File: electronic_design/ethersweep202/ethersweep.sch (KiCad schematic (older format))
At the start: 88 parts, among them J1 AVR-ISP-6, J10 HR911105A, J2 Conn_01x02_Male, J3 Conn_01x04_Female, J4 Conn_01x02_Male, J5 Conn_01x02_Male, J7 Conn_01x06_Female, J8 AVR-ISP-6, J9 Conn_01x06_Male, M1 Stepper_Motor_bipolar, SW1 SW_Push, U2 ATmega328-AU, U3 DRV8825PWPR, U4 AMS1117-3.3, U5 AS5600, U6 W5500, Y2 Crystal_25MHz, Y3 Crystal

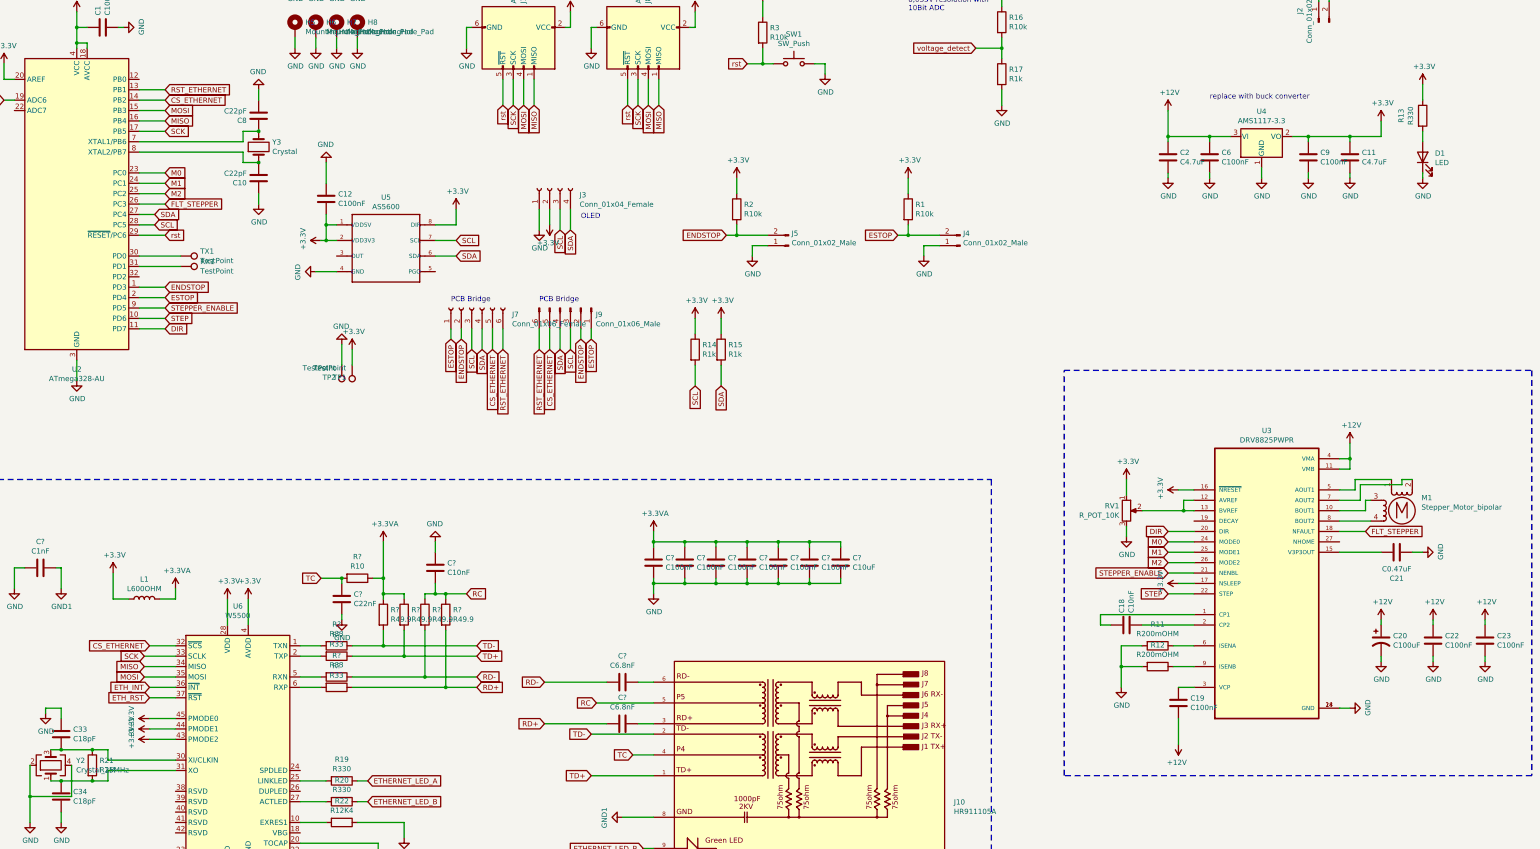
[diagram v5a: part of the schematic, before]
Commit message: added interrupt pin to w5500
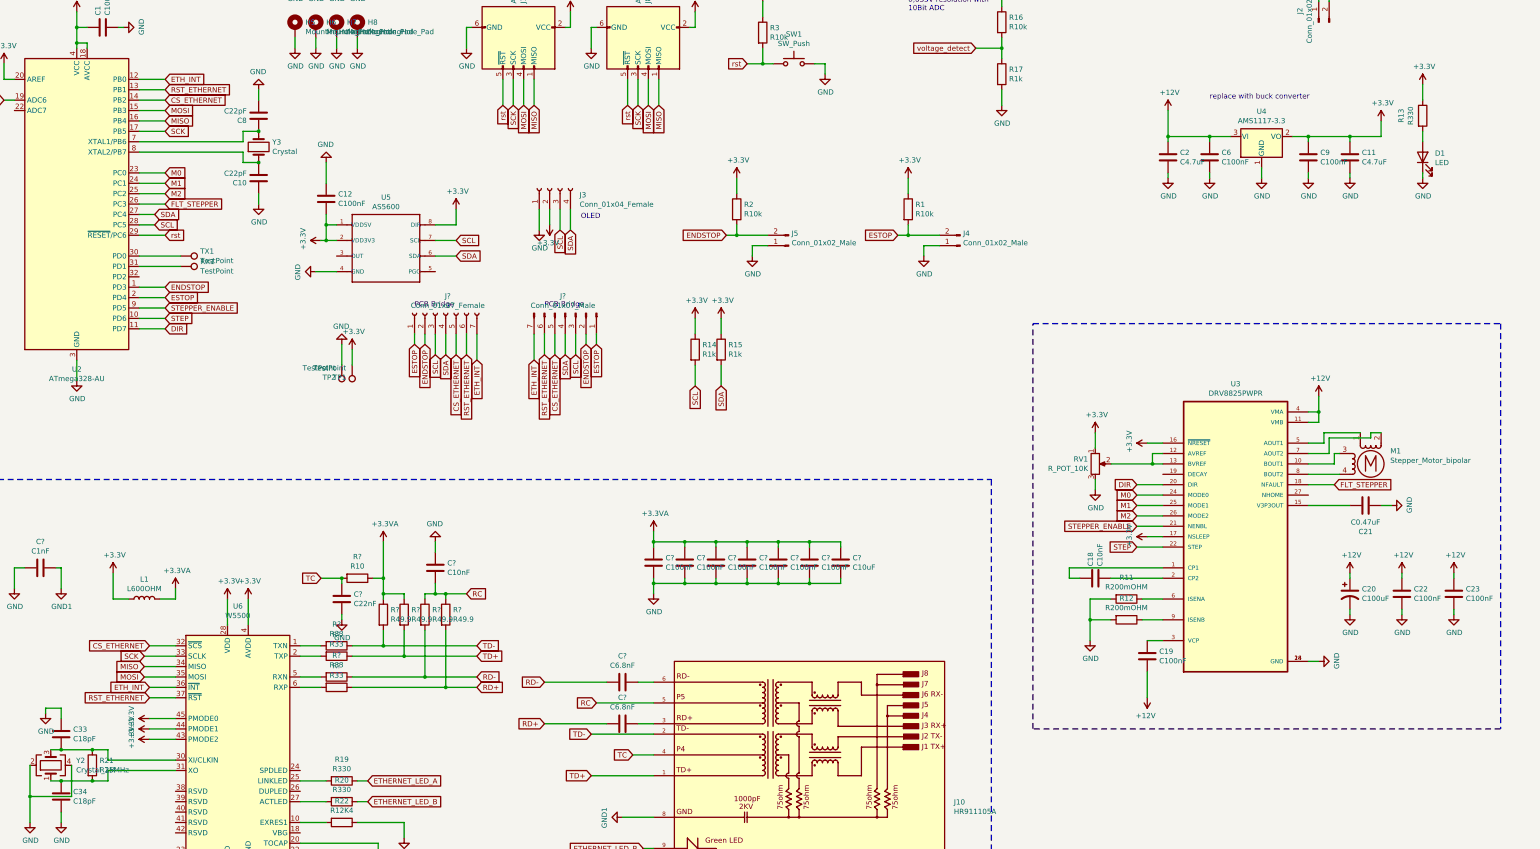
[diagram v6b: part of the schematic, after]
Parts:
- removed J7: Conn_01x06_Female, Connector_PinHeader_2.54mm:PinHeader_1x06_P2.54mm_Vertical, symbol Connector:Conn_01x06_Female
- removed J9: Conn_01x06_Male, Connector_PinHeader_2.54mm:PinHeader_1x06_P2.54mm_Vertical, symbol Connector:Conn_01x06_Male
- added J?: Conn_01x07_Male, symbol Connector:Conn_01x07_Male
- added J?: Conn_01x07_Female, symbol Connector:Conn_01x07_Female
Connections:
- net ETH_RST is gone; now on net RST_ETHERNET: U6.37 (~RST)
- net CS_ETHERNET: now also J?.5 (Pin_5), J?.5 (Pin_5)
- net ENDSTOP: now also J?.2 (Pin_2), J?.2 (Pin_2)
- net ESTOP: now also J?.1 (Pin_1), J?.1 (Pin_1)
- net ETH_INT: now also U2.12 (PB0), J?.7 (Pin_7), J?.7 (Pin_7)
- net RST_ETHERNET: now also J?.6 (Pin_6), J?.6 (Pin_6)
- net SCL: now also J?.3 (Pin_3), J?.3 (Pin_3)
- net SDA: now also J?.4 (Pin_4), J?.4 (Pin_4)
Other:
- moved on the sheet: C18, C19, C20, C21, C22, C23, M1, R11, R12, RV1, U3

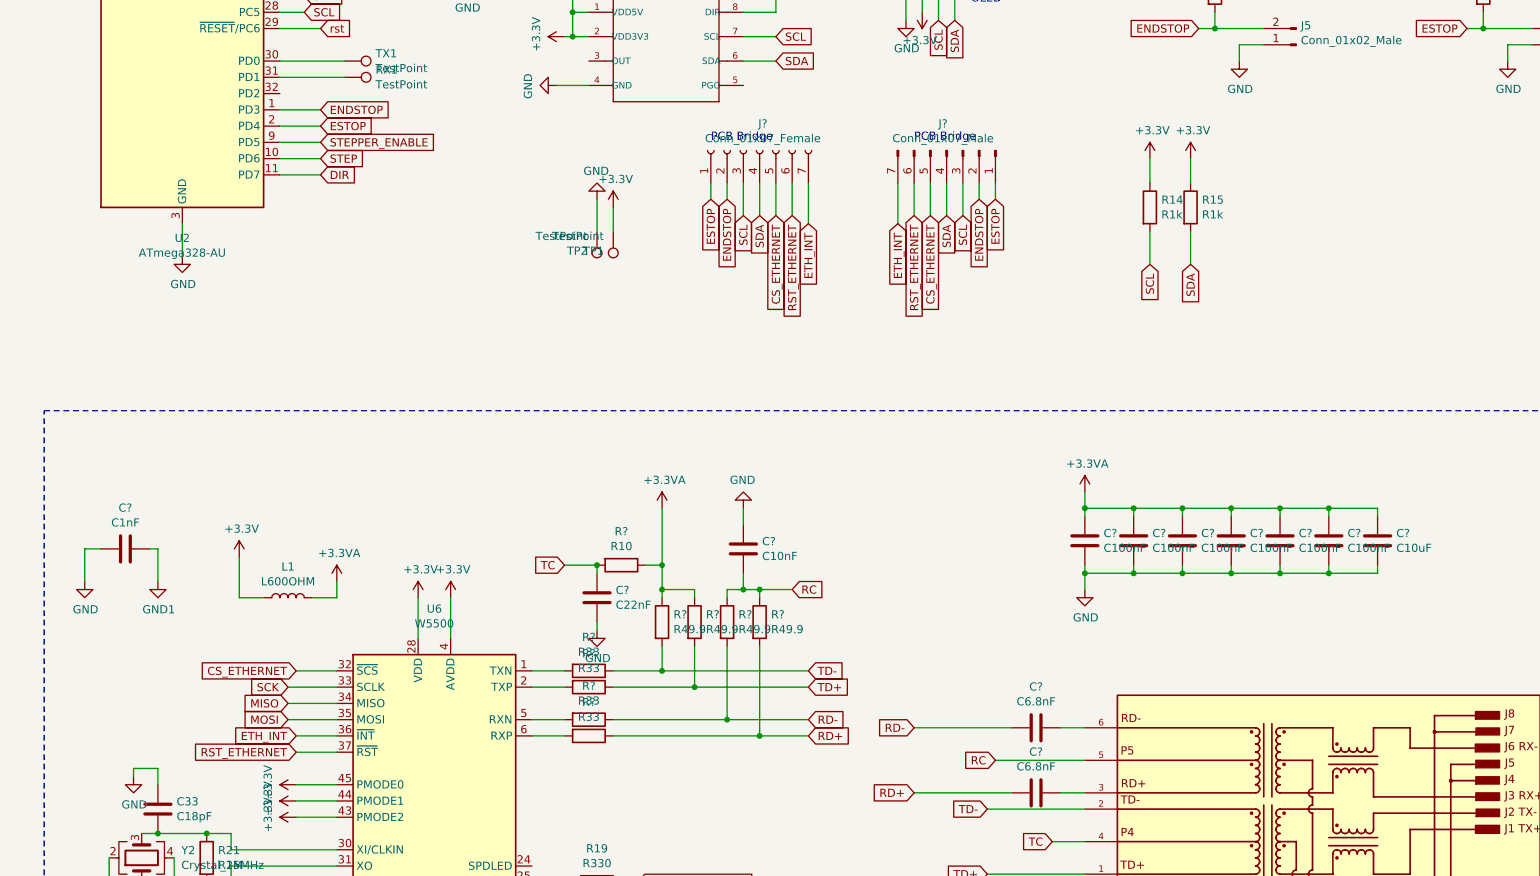
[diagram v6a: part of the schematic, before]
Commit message: layout implementation board 1 done, board 2 in progress
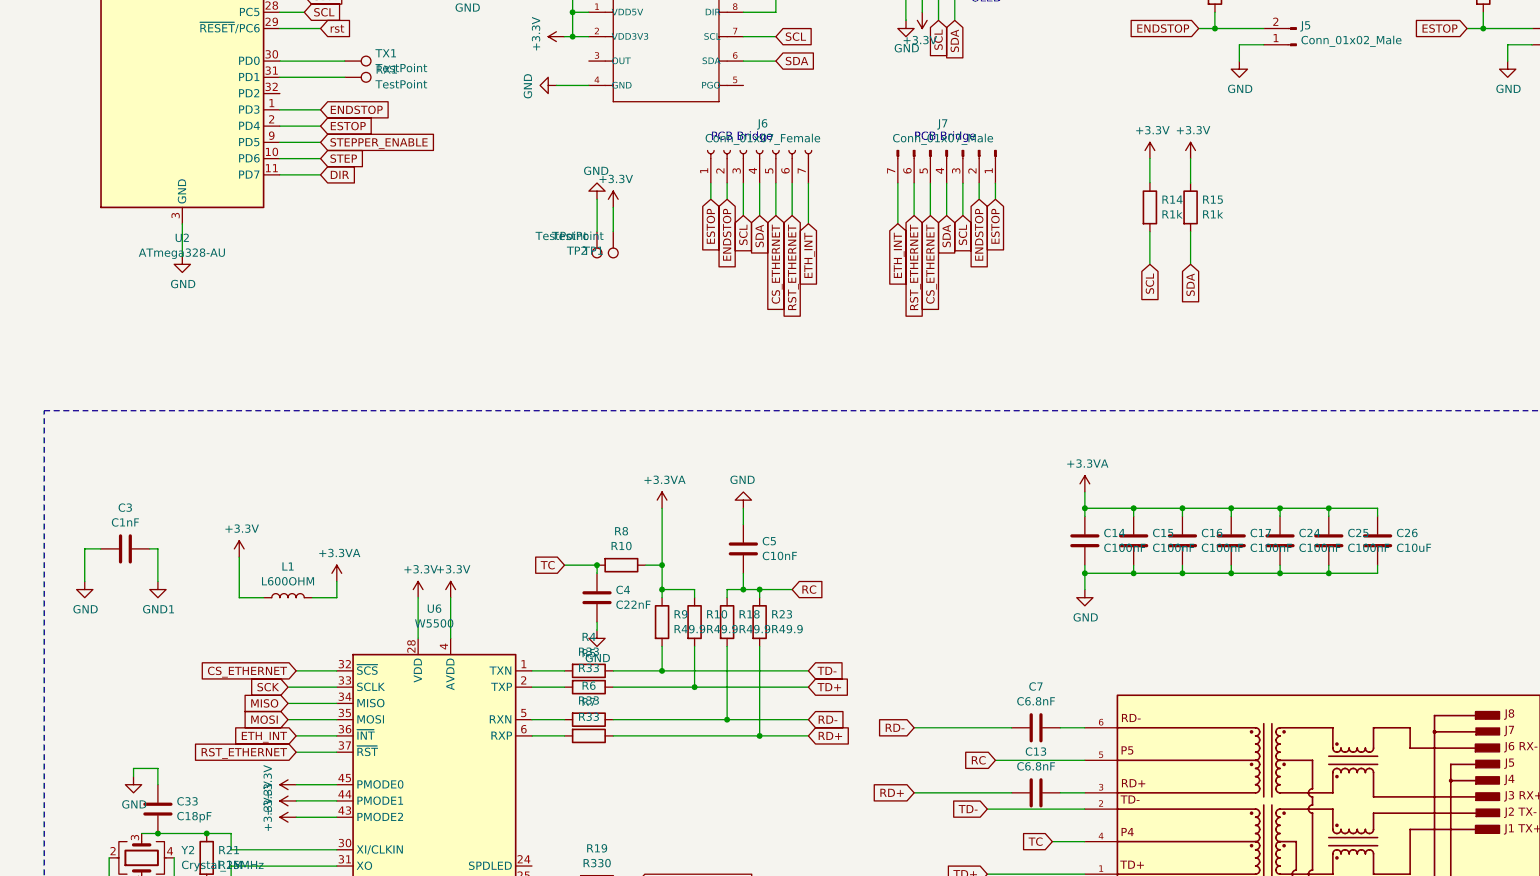
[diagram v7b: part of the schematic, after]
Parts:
- J6, J7: renamed from J?; footprint (none) -> Connector_PinHeader_2.54mm:PinHeader_1x07_P2.54mm_Vertical
- L1: footprint (none) -> Inductor_SMD:L_0805_2012Metric
- gave numbers to parts that had none: 21
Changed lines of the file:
@@
 F 0 "L1" V 2790 6950 50  0000 C CNN
 F 1 "L600OHM" V 2699 6950 50  0000 C CNN
-F 2 "" H 2600 6950 50  0001 C CNN
+F 2 "Inductor_SMD:L_0805_2012Metric" H 2600 6950 50  0001 C CNN
 F 3 "~" H 2600 6950 50  0001 C CNN
 F 4 "C1017" V 2600 6950 50  0001 C CNN "LCSC"
@@
 	5100 9100 5100 9250
 $Comp
-L power:GND1 #PWR?
+L power:GND1 #PWR0109
 U 1 1 614FEAD4
 P 1800 6850
-F 0 "#PWR?" H 1800 6600 50  0001 C CNN
+F 0 "#PWR0109" H 1800 6600 50  0001 C CNN
 F 1 "GND1" H 1805 6677 50  0000 C CNN
 F 2 "" H 1800 6850 50  0001 C CNN
@@
 $EndComp
 $Comp
-L power:GND #PWR?
+L power:GND #PWR0115
 U 1 1 6152709E
 P 1350 6850
-F 0 "#PWR?" H 1350 6600 50  0001 C CNN
+F 0 "#PWR0115" H 1350 6600 50  0001 C CNN
 F 1 "GND" H 1355 6677 50  0000 C CNN
 F 2 "" H 1350 6850 50  0001 C CNN
@@
 $EndComp
 $Comp
-L Device:C C?
+L Device:C C3
 U 1 1 61578613
 P 1600 6650
-F 0 "C?" V 1348 6650 50  0000 C CNN
+F 0 "C3" V 1348 6650 50  0000 C CNN
 F 1 "C1nF" V 1439 6650 50  0000 C CNN
 F 2 "Resistor_SMD:R_1206_3216Metric" H 1638 6500 50  0001 C CNN
@@
 	1800 6650 1800 6850
 $Comp
-L Device:C C?
+L Device:C C13
 U 1 1 615FC292
 P 7200 8150
-F 0 "C?" V 6948 8150 50  0000 C CNN
+F 0 "C13" V 6948 8150 50  0000 C CNN
 F 1 "C6.8nF" V 7039 8150 50  0000 C CNN
 F 2 "Resistor_SMD:R_0402_1005Metric" H 7238 8000 50  0001 C CNN
@@
 $EndComp
 $Comp
-L Device:C C?
+L Device:C C7
 U 1 1 615FE6F7
 P 7200 7750
-F 0 "C?" V 6948 7750 50  0000 C CNN
+F 0 "C7" V 6948 7750 50  0000 C CNN
 F 1 "C6.8nF" V 7039 7750 50  0000 C CNN
 F 2 "Resistor_SMD:R_0402_1005Metric" H 7238 7600 50  0001 C CNN
@@
 	7350 8150 7500 8150
 $Comp
-L Device:R R?
+L Device:R R4
 U 1 1 6179C9A4
 P 4450 7400
-F 0 "R?" V 4243 7400 50  0000 C CNN
+F 0 "R4" V 4243 7400 50  0000 C CNN
 F 1 "R33" V 4334 7400 50  0000 C CNN
 F 2 "Resistor_SMD:R_0805_2012Metric" V 4380 7400 50  0001 C CNN
@@
 $EndComp
 $Comp
-L Device:R R?
+L Device:R R5
 U 1 1 6179EB6B
 P 4450 7500
-F 0 "R?" V 4243 7500 50  0000 C CNN
+F 0 "R5" V 4243 7500 50  0000 C CNN
 F 1 "R33" V 4334 7500 50  0000 C CNN
 F 2 "Resistor_SMD:R_0805_2012Metric" V 4380 7500 50  0001 C CNN
@@
 $EndComp
 $Comp
-L Device:R R?
+L Device:R R6
 U 1 1 617C8079
 P 4450 7700
-F 0 "R?" V 4243 7700 50  0000 C CNN
+F 0 "R6" V 4243 7700 50  0000 C CNN
 F 1 "R33" V 4334 7700 50  0000 C CNN
 F 2 "Resistor_SMD:R_0805_2012Metric" V 4380 7700 50  0001 C CNN
@@
 $EndComp
 $Comp
-L Device:R R?
+L Device:R R7
 U 1 1 617C8080
 P 4450 7800
-F 0 "R?" V 4243 7800 50  0000 C CNN
+F 0 "R7" V 4243 7800 50  0000 C CNN
 F 1 "R33" V 4334 7800 50  0000 C CNN
 F 2 "Resistor_SMD:R_0805_2012Metric" V 4380 7800 50  0001 C CNN
@@
 	4300 7800 4100 7800
 $Comp
-L Device:R R?
+L Device:R R10
 U 1 1 618C73B2
 P 5100 7100
-F 0 "R?" H 5170 7146 50  0000 L CNN
+F 0 "R10" H 5170 7146 50  0000 L CNN
 F 1 "R49.9" H 5170 7055 50  0000 L CNN
 F 2 "Resistor_SMD:R_0603_1608Metric" V 5030 7100 50  0001 C CNN
@@
 $EndComp
 $Comp
-L Device:R R?
+L Device:R R9
 U 1 1 618F356F
 P 4900 7100
-F 0 "R?" H 4970 7146 50  0000 L CNN
+F 0 "R9" H 4970 7146 50  0000 L CNN
 F 1 "R49.9" H 4970 7055 50  0000 L CNN
 F 2 "Resistor_SMD:R_0603_1608Metric" V 4830 7100 50  0001 C CNN
@@
 $EndComp
 $Comp
-L Device:R R?
+L Device:R R18
 U 1 1 6191D5B6
 P 5300 7100
-F 0 "R?" H 5370 7146 50  0000 L CNN
+F 0 "R18" H 5370 7146 50  0000 L CNN
 F 1 "R49.9" H 5370 7055 50  0000 L CNN
 F 2 "Resistor_SMD:R_0603_1608Metric" V 5230 7100 50  0001 C CNN
@@
 $EndComp
 $Comp
-L Device:R R?
+L Device:R R23
 U 1 1 619474DF
 P 5500 7100
-F 0 "R?" H 5570 7146 50  0000 L CNN
+F 0 "R23" H 5570 7146 50  0000 L CNN
 F 1 "R49.9" H 5570 7055 50  0000 L CNN
 F 2 "Resistor_SMD:R_0603_1608Metric" V 5430 7100 50  0001 C CNN
@@
 	5500 6900 5500 6950
 $Comp
-L Device:R R?
+L Device:R R8
 U 1 1 61B5EFE1
 P 4650 6750
-F 0 "R?" V 4443 6750 50  0000 C CNN
+F 0 "R8" V 4443 6750 50  0000 C CNN
 F 1 "R10" V 4534 6750 50  0000 C CNN
 F 2 "Resistor_SMD:R_0805_2012Metric" V 4580 6750 50  0001 C CNN
@@
 $EndComp
 $Comp
-L Device:C C?
+L Device:C C4
 U 1 1 61B62CF8
 P 4500 6950
-F 0 "C?" H 4385 6904 50  0000 R CNN
+F 0 "C4" H 4385 6904 50  0000 R CNN
 F 1 "C22nF" H 4385 6995 50  0000 R CNN
 F 2 "Resistor_SMD:R_0603_1608Metric" H 4538 6800 50  0001 C CNN
@@
 	4500 7100 4500 7150
 $Comp
-L power:GND #PWR?
+L power:GND #PWR0123
 U 1 1 61B90760
 P 4500 7150
-F 0 "#PWR?" H 4500 6900 50  0001 C CNN
+F 0 "#PWR0123" H 4500 6900 50  0001 C CNN
 F 1 "GND" H 4505 6977 50  0000 C CNN
 F 2 "" H 4500 7150 50  0001 C CNN
@@
 Connection ~ 4900 6900
 $Comp
-L Device:C C?
+L Device:C C5
 U 1 1 61D66F5A
 P 5400 6650
-F 0 "C?" H 5515 6696 50  0000 L CNN
+F 0 "C5" H 5515 6696 50  0000 L CNN
 F 1 "C10nF" H 5515 6605 50  0000 L CNN
 F 2 "Capacitor_SMD:C_0603_1608Metric" H 5438 6500 50  0001 C CNN
@@
 	5400 6900 5500 6900
 $Comp
-L power:GND #PWR?
+L power:GND #PWR0125
 U 1 1 61DF78D8
 P 5400 6400
-F 0 "#PWR?" H 5400 6150 50  0001 C CNN
+F 0 "#PWR0125" H 5400 6150 50  0001 C CNN
 F 1 "GND" H 5405 6227 50  0000 C CNN
 F 2 "" H 5400 6400 50  0001 C CNN
@@
 $EndComp
 $Comp
-L power:+3.3VA #PWR?
+L power:+3.3VA #PWR0131
 U 1 1 61E2787D
 P 4900 6400
-F 0 "#PWR?" H 4900 6250 50  0001 C CNN
+F 0 "#PWR0131" H 4900 6250 50  0001 C CNN
 F 1 "+3.3VA" H 4915 6573 50  0000 C CNN
 F 2 "" H 4900 6400 50  0001 C CNN
@@
 	4900 6400 4900 6750
 $Comp
-L power:GND #PWR?
+L power:GND #PWR0132
 U 1 1 6241D47E
 P 7500 6900
-F 0 "#PWR?" H 7500 6650 50  0001 C CNN
+F 0 "#PWR0132" H 7500 6650 50  0001 C CNN
 F 1 "GND" H 7505 6727 50  0000 C CNN
 F 2 "" H 7500 6900 50  0001 C CNN
@@
 $EndComp
 $Comp
-L Device:C C?
+L Device:C C14
 U 1 1 6241D487
 P 7500 6600
-F 0 "C?" H 7615 6646 50  0000 L CNN
+F 0 "C14" H 7615 6646 50  0000 L CNN
 F 1 "C100nF" H 7615 6555 50  0000 L CNN
 F 2 "Capacitor_SMD:C_0402_1005Metric" H 7538 6450 50  0001 C CNN
@@
 $EndComp
 $Comp
-L Device:C C?
+L Device:C C15
 U 1 1 6244E413
 P 7800 6600
-F 0 "C?" H 7915 6646 50  0000 L CNN
+F 0 "C15" H 7915 6646 50  0000 L CNN
 F 1 "C100nF" H 7915 6555 50  0000 L CNN
 F 2 "Capacitor_SMD:C_0402_1005Metric" H 7838 6450 50  0001 C CNN
@@
 $EndComp
 $Comp
-L Device:C C?
+L Device:C C16
 U 1 1 6247F4F3
 P 8100 6600
-F 0 "C?" H 8215 6646 50  0000 L CNN
+F 0 "C16" H 8215 6646 50  0000 L CNN
 F 1 "C100nF" H 8215 6555 50  0000 L CNN
 F 2 "Capacitor_SMD:C_0402_1005Metric" H 8138 6450 50  0001 C CNN
@@
 $EndComp
 $Comp
-L Device:C C?
+L Device:C C17
 U 1 1 6247F4FA
 P 8400 6600
-F 0 "C?" H 8515 6646 50  0000 L CNN
+F 0 "C17" H 8515 6646 50  0000 L CNN
 F 1 "C100nF" H 8515 6555 50  0000 L CNN
 F 2 "Capacitor_SMD:C_0402_1005Metric" H 8438 6450 50  0001 C CNN
@@
 $EndComp
 $Comp
-L Device:C C?
+L Device:C C24
 U 1 1 624B0E42
 P 8700 6600
-F 0 "C?" H 8815 6646 50  0000 L CNN
+F 0 "C24" H 8815 6646 50  0000 L CNN
 F 1 "C100nF" H 8815 6555 50  0000 L CNN
 F 2 "Capacitor_SMD:C_0402_1005Metric" H 8738 6450 50  0001 C CNN
@@
 $EndComp
 $Comp
-L Device:C C?
+L Device:C C25
 U 1 1 624B0E49
 P 9000 6600
-F 0 "C?" H 9115 6646 50  0000 L CNN
+F 0 "C25" H 9115 6646 50  0000 L CNN
 F 1 "C100nF" H 9115 6555 50  0000 L CNN
 F 2 "Capacitor_SMD:C_0402_1005Metric" H 9038 6450 50  0001 C CNN
@@
 	9000 6800 9300 6800
 $Comp
-L Device:C C?
+L Device:C C26
 U 1 1 628565B2
 P 9300 6600
-F 0 "C?" H 9415 6646 50  0000 L CNN
+F 0 "C26" H 9415 6646 50  0000 L CNN
 F 1 "C10uF" H 9415 6555 50  0000 L CNN
 F 2 "Capacitor_SMD:C_0805_2012Metric" H 9338 6450 50  0001 C CNN
@@
 $EndComp
 $Comp
-L power:+3.3VA #PWR?
+L power:+3.3VA #PWR0133
 U 1 1 629A7A7D
 P 7500 6300
-F 0 "#PWR?" H 7500 6150 50  0001 C CNN
+F 0 "#PWR0133" H 7500 6150 50  0001 C CNN
 F 1 "+3.3VA" H 7515 6473 50  0000 C CNN
 F 2 "" H 7500 6300 50  0001 C CNN
@@
 RST_ETHERNET
 $Comp
-L Connector:Conn_01x07_Male J?
+L Connector:Conn_01x07_Male J7
 U 1 1 62F76875
 P 6650 4200
-F 0 "J?" V 6485 4178 50  0000 C CNN
+F 0 "J7" V 6485 4178 50  0000 C CNN
 F 1 "Conn_01x07_Male" V 6576 4178 50  0000 C CNN
-F 2 "" H 6650 4200 50  0001 C CNN
+F 2 "Connector_PinHeader_2.54mm:PinHeader_1x07_P2.54mm_Vertical" H 6650 4200 50  0001 C CNN
 F 3 "~" H 6650 4200 50  0001 C CNN
 	1    6650 4200
@@
 $EndComp
 $Comp
-L Connector:Conn_01x07_Female J?
+L Connector:Conn_01x07_Female J6
 U 1 1 62FB7670
 P 5500 4200
-F 0 "J?" V 5665 4180 50  0000 C CNN
+F 0 "J6" V 5665 4180 50  0000 C CNN
 F 1 "Conn_01x07_Female" V 5574 4180 50  0000 C CNN
-F 2 "" H 5500 4200 50  0001 C CNN
+F 2 "Connector_PinHeader_2.54mm:PinHeader_1x07_P2.54mm_Vertical" H 5500 4200 50  0001 C CNN
 F 3 "~" H 5500 4200 50  0001 C CNN
 	1    5500 4200

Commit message: design and layout changes
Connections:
- net RD+: now also C13.1, J10.3; no longer C13.2, R23.2, R7.1
- net RD-: now also C7.1, J10.6; no longer C7.2, R18.2, R6.1
- new net: C13.2, R23.2, R7.1
- new net: C7.2, R18.2, R6.1
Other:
- moved on the sheet: C13, C7
